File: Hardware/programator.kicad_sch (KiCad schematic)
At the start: 1 part, among them U32 STLINK-V3MODS

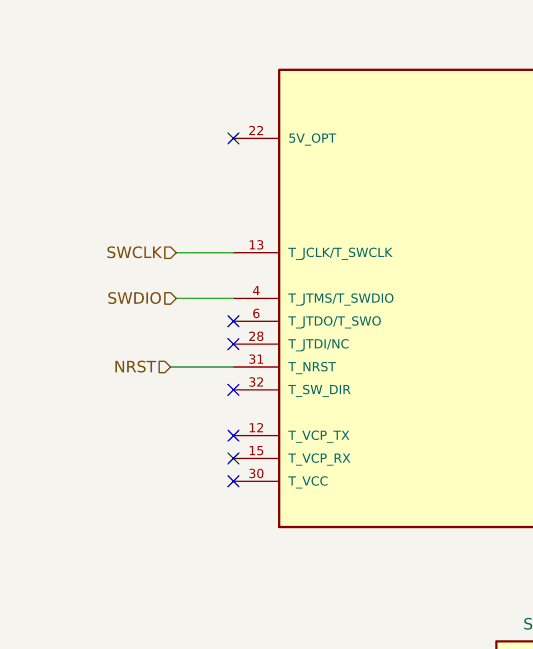
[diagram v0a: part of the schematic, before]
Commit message: Changes in current layout, added tensometers to layout
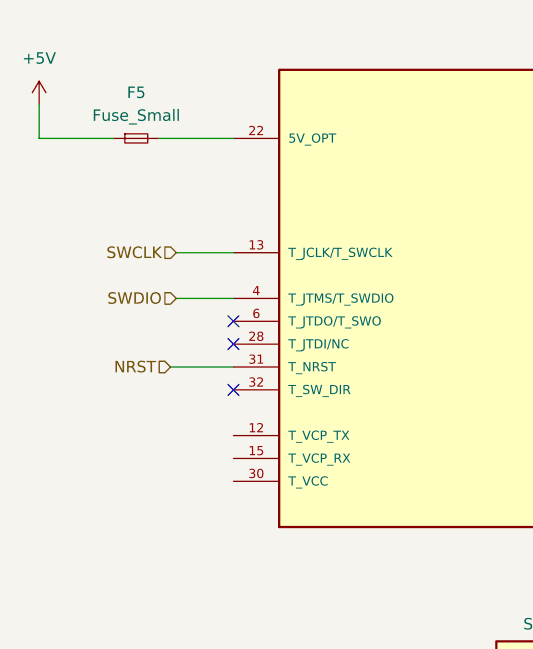
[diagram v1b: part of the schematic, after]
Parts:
- added F5: Fuse_Small, Fuse:Fuse_0805_2012Metric, symbol Device:Fuse_Small
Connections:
- net at U32.22 (5V_OPT): now also F5.2
- new net +5V: F5.1
- no-connect marks 23 -> 19
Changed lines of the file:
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@@
-	)
-	(no_connect
-		(at 90.805 102.87)
 	)
 	(no_connect
@@
 	)
 	(no_connect
-		(at 90.805 107.95)
-	)
-	(no_connect
 		(at 172.085 85.09)
 	)
 	(no_connect
-		(at 90.805 69.85)
-	)
-	(no_connect
 		(at 90.805 90.17)
 	)
@@
 		(at 172.085 92.71)
 	)
-	(no_connect
-		(at 90.805 105.41)
-	)
 	(wire
 		(pts
@@
 	(wire
 		(pts
+			(xy 82.55 69.85) (xy 90.805 69.85)
+		)
+		(stroke
+			(width 0)
+			(type default)
+		)
+	)
+	(wire
+		(pts
+			(xy 69.215 66.04) (xy 69.215 69.85)
+		)
+		(stroke
+			(width 0)
+			(type default)
+		)
+	)
+	(wire
+		(pts
 			(xy 84.455 87.63) (xy 90.805 87.63)
 		)
@@
 		(pts
 			(xy 145.415 138.43) (xy 145.415 140.97)
+		)
+		(stroke
+			(width 0)
+			(type default)
+		)
+	)
+	(wire
+		(pts
+			(xy 69.215 69.85) (xy 77.47 69.85)
 		)
 		(stroke
@@
 	)
 	(symbol
+		(lib_id "power:+5V")
+		(at 69.215 66.04 0)
+		(unit 1)
+		(exclude_from_sim no)
+		(in_bom yes)
+		(on_board yes)
+		(dnp no)
+		(property "Reference" "#PWR09"
+			(at 69.215 69.85 0)
+			(effects
+				(font
+					(size 1.27 1.27)
+				)
+				(hide yes)
+			)
+		)
+		(property "Value" "+5V"
+			(at 69.215 60.96 0)
+			(effects
+				(font
+					(size 1.27 1.27)
+				)
+			)
+		)
+		(property "Footprint" ""
+			(at 69.215 66.04 0)
+			(effects
+				(font
+					(size 1.27 1.27)
+				)
+				(hide yes)
+			)
+		)
+		(property "Datasheet" ""
+			(at 69.215 66.04 0)
+			(effects
+				(font
+					(size 1.27 1.27)
+				)
+				(hide yes)
+			)
+		)
+		(property "Description" ""
+			(at 69.215 66.04 0)
+			(effects
+				(font
+					(size 1.27 1.27)
+				)
+				(hide yes)
+			)
+		)
+		(pin "1"
+		)
+		(instances
+			(project "PUTM_EV_Frontbox_2023"
+				(path "/b652b05a-4e3d-4ad1-b032-18886abe7d45/dd0098ec-f4e0-48aa-9050-ddfd0a2e4304"
+					(reference "#PWR09")
+					(unit 1)
+				)
+			)
+		)
+	)
+	(symbol
 		(lib_id "FrontBox:STLINK-V3MODS")
 		(at 131.445 87.63 0)
@@
 					(unit 1)
 				)
+			)
+		)
+	)
+	(symbol
+		(lib_id "Device:Fuse_Small")
+		(at 80.01 69.85 0)
+		(unit 1)
+		(exclude_from_sim no)
+		(in_bom yes)
+		(on_board yes)
+		(dnp no)
+		(fields_autoplaced yes)
+		(property "Reference" "F5"
+			(at 80.01 64.77 0)
+			(effects
+				(font
+					(size 1.27 1.27)
+				)
+			)
+		)
+		(property "Value" "Fuse_Small"
+			(at 80.01 67.31 0)
+			(effects
+				(font
+					(size 1.27 1.27)
+				)
+			)
+		)
+		(property "Footprint" "Fuse:Fuse_0805_2012Metric"
+			(at 80.01 69.85 0)
+			(effects
+				(font
+					(size 1.27 1.27)
+				)
+				(hide yes)
+			)
+		)
+		(property "Datasheet" "~"
+			(at 80.01 69.85 0)
+			(effects
+				(font
+					(size 1.27 1.27)
+				)
+				(hide yes)
+			)
+		)
+		(property "Description" "Fuse, small symbol"
+			(at 80.01 69.85 0)
+			(effects
+				(font
+					(size 1.27 1.27)
+				)
+				(hide yes)
+			)
+		)
+		(pin "2"
+		)
+		(pin "1"
+		)
+		(instances
+			(project "PUTM_EV_Frontbox_2023"
+				(path "/b652b05a-4e3d-4ad1-b032-18886abe7d45/dd0098ec-f4e0-48aa-9050-ddfd0a2e4304"
+					(reference "F5")
+					(unit 1)
+				)

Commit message: Frontbox 2025 Version 1.0
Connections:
- no-connect marks 19 -> 22
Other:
- moved on the sheet: U32A
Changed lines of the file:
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@@
 	)
 	(no_connect
-		(at 90.805 92.71)
-	)
-	(no_connect
-		(at 172.085 105.41)
-	)
-	(no_connect
-		(at 172.085 74.93)
-	)
-	(no_connect
-		(at 172.085 72.39)
-	)
-	(no_connect
-		(at 172.085 87.63)
-	)
-	(no_connect
-		(at 172.085 85.09)
-	)
-	(no_connect
-		(at 90.805 90.17)
-	)
-	(no_connect
-		(at 172.085 107.95)
-	)
-	(no_connect
-		(at 172.085 77.47)
-	)
-	(no_connect
-		(at 172.085 80.01)
-	)
-	(no_connect
-		(at 172.085 95.25)
-	)
-	(no_connect
-		(at 172.085 100.33)
-	)
-	(no_connect
-		(at 90.805 97.79)
-	)
-	(no_connect
-		(at 172.085 82.55)
-	)
-	(no_connect
-		(at 172.085 90.17)
-	)
-	(no_connect
-		(at 172.085 102.87)
-	)
-	(no_connect
-		(at 172.085 69.85)
-	)
-	(no_connect
-		(at 172.085 97.79)
-	)
-	(no_connect
-		(at 172.085 92.71)
+		(at 91.44 92.71)
+	)
+	(no_connect
+		(at 91.44 107.95)
+	)
+	(no_connect
+		(at 91.44 102.87)
+	)
+	(no_connect
+		(at 172.72 105.41)
+	)
+	(no_connect
+		(at 172.72 74.93)
+	)
+	(no_connect
+		(at 172.72 72.39)
+	)
+	(no_connect
+		(at 172.72 87.63)
+	)
+	(no_connect
+		(at 172.72 85.09)
+	)
+	(no_connect
+		(at 91.44 90.17)
+	)
+	(no_connect
+		(at 172.72 107.95)
+	)
+	(no_connect
+		(at 172.72 77.47)
+	)
+	(no_connect
+		(at 172.72 80.01)
+	)
+	(no_connect
+		(at 172.72 95.25)
+	)
+	(no_connect
+		(at 172.72 100.33)
+	)
+	(no_connect
+		(at 91.44 105.41)
+	)
+	(no_connect
+		(at 91.44 97.79)
+	)
+	(no_connect
+		(at 172.72 82.55)
+	)
+	(no_connect
+		(at 172.72 90.17)
+	)
+	(no_connect
+		(at 172.72 102.87)
+	)
+	(no_connect
+		(at 172.72 69.85)
+	)
+	(no_connect
+		(at 172.72 97.79)
+	)
+	(no_connect
+		(at 172.72 92.71)
 	)
 	(wire
@@
 	(wire
 		(pts
-			(xy 82.55 69.85) (xy 90.805 69.85)
-		)
-		(stroke
-			(width 0)
-			(type default)
-		)
-	)
-	(wire
-		(pts
-			(xy 69.215 66.04) (xy 69.215 69.85)
-		)
-		(stroke
-			(width 0)
-			(type default)
-		)
-	)
-	(wire
-		(pts
-			(xy 84.455 87.63) (xy 90.805 87.63)
+			(xy 82.55 69.85) (xy 91.44 69.85)
+		)
+		(stroke
+			(width 0)
+			(type default)
+		)
+	)
+	(wire
+		(pts
+			(xy 69.85 66.04) (xy 69.85 69.85)
+		)
+		(stroke
+			(width 0)
+			(type default)
+		)
+	)
+	(wire
+		(pts
+			(xy 85.09 87.63) (xy 91.44 87.63)
 		)
 		(stroke
@@
 	(wire
 		(pts
-			(xy 69.215 69.85) (xy 77.47 69.85)
+			(xy 69.85 69.85) (xy 77.47 69.85)
 		)
 		(stroke
@@
 	(wire
 		(pts
-			(xy 83.82 95.25) (xy 90.805 95.25)
-		)
-		(stroke
-			(width 0)
-			(type default)
-		)
-	)
-	(wire
-		(pts
-			(xy 84.455 82.55) (xy 90.805 82.55)
+			(xy 83.82 95.25) (xy 91.44 95.25)
+		)
+		(stroke
+			(width 0)
+			(type default)
+		)
+	)
+	(wire
+		(pts
+			(xy 85.09 82.55) (xy 91.44 82.55)
 		)
 		(stroke
@@
 	(hierarchical_label "SWDIO"
 		(shape input)
-		(at 84.455 87.63 180)
+		(at 85.09 87.63 180)
 		(fields_autoplaced yes)
 		(effects
@@
 	(hierarchical_label "SWCLK"
 		(shape input)
-		(at 84.455 82.55 180)
+		(at 85.09 82.55 180)
 		(fields_autoplaced yes)
 		(effects
@@
 	(symbol
 		(lib_id "power:+5V")
-		(at 69.215 66.04 0)
+		(at 69.85 66.04 0)
 		(unit 1)
 		(exclude_from_sim no)
@@
 		(dnp no)
 		(property "Reference" "#PWR09"
-			(at 69.215 69.85 0)
+			(at 69.85 69.85 0)
 			(effects
 				(font
@@
 		)
 		(property "Value" "+5V"
-			(at 69.215 60.96 0)
+			(at 69.85 60.96 0)
 			(effects
 				(font
@@
 		)
 		(property "Footprint" ""
-			(at 69.215 66.04 0)
+			(at 69.85 66.04 0)
 			(effects
 				(font
@@
 		)
 		(property "Datasheet" ""
-			(at 69.215 66.04 0)
+			(at 69.85 66.04 0)
 			(effects
 				(font
@@
 		)
 		(property "Description" ""
-			(at 69.215 66.04 0)
+			(at 69.85 66.04 0)
 			(effects
 				(font
@@
 	(symbol
 		(lib_id "FrontBox:STLINK-V3MODS")
-		(at 131.445 87.63 0)
+		(at 132.08 87.63 0)
 		(unit 1)
 		(exclude_from_sim no)
@@
 		(fields_autoplaced yes)
 		(property "Reference" "U32"
-			(at 131.445 57.785 0)
+			(at 132.08 57.785 0)
 			(effects
 				(font
@@
 		)
 		(property "Value" "STLINK-V3MODS"
-			(at 131.445 60.325 0)
+			(at 132.08 60.325 0)
 			(effects
 				(font
@@
 		)
 		(property "Footprint" "Frontbox:MODULE_STLINK-V3MODS"
-			(at 131.445 87.63 0)
+			(at 132.08 87.63 0)
 			(effects
 				(font
@@
 		)
 		(property "Datasheet" ""
-			(at 131.445 87.63 0)
+			(at 132.08 87.63 0)
 			(effects
 				(font
@@
 		)
 		(property "Description" "STM32 series Debugger, Programmer (In-Circuit/In-System)"
-			(at 131.445 87.63 0)
+			(at 132.08 87.63 0)
 			(effects
 				(font
@@
 		)
 		(property "DigiKey_Part_Number" "497-STLINK-V3MODS-ND"
-			(at 131.445 87.63 0)
+			(at 132.08 87.63 0)
 			(effects
 				(font
@@
 		)
 		(property "MF" "STMicroelectronics"
-			(at 131.445 87.63 0)
+			(at 132.08 87.63 0)
 			(effects
 				(font
@@
 		)
 		(property "Purchase-URL" "https://www.snapeda.com/api/url_track_click_mouser/?unipart_id=4704654&manufacturer=STMicroelectronics&part_name=STLINK-V3MODS&search_term=stlink-v3mods"
-			(at 131.445 87.63 0)
+			(at 132.08 87.63 0)
 			(effects
 				(font
@@
 		)
 		(property "Package" "None"
-			(at 131.445 87.63 0)
+			(at 132.08 87.63 0)
 			(effects
 				(font
@@
 		)
 		(property "Check_prices" "https://www.snapeda.com/parts/STLINK-V3MODS/STMicroelectronics/view-part/?ref=eda"
-			(at 131.445 87.63 0)
+			(at 132.08 87.63 0)
 			(effects
 				(font
@@
 		)
 		(property "STANDARD" "Manufacturer Recommendations"
-			(at 131.445 87.63 0)
+			(at 132.08 87.63 0)
 			(effects
 				(font
@@
 		)
 		(property "PARTREV" "1"
-			(at 131.445 87.63 0)
+			(at 132.08 87.63 0)
 			(effects
 				(font
@@
 		)
 		(property "SnapEDA_Link" "https://www.snapeda.com/parts/STLINK-V3MODS/STMicroelectronics/view-part/?ref=snap"
-			(at 131.445 87.63 0)
+			(at 132.08 87.63 0)
 			(effects
 				(font
@@
 		)
 		(property "MP" "STLINK-V3MODS"
-			(at 131.445 87.63 0)
+			(at 132.08 87.63 0)
 			(effects
 				(font
@@
 		)
 		(property "MANUFACTURER" "ST Microelectronics"
-			(at 131.445 87.63 0)
-			(effects
-				(font
+			(at 132.08 87.63 0)
+			(effects
+				(font
